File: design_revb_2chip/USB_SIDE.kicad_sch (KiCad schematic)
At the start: 53 parts, among them J1 USB_C_Receptacle, J2 Conn_01x08, U1 LAN7801-I/9JX, U2 TPS62162QDSGRQ1, U3 93C56A-I/P

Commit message: USB_Side Prelim Completion
- finished USB side with no revisions
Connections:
- net 3.3V is gone; now on net 3v3: C21.1, D2.2 (A), L2.2, R11.2, R9.2, U2.6 (VOS)
- net GPIO10: now also J2.1 (Pin_1); no longer J2.7 (Pin_7)
- net GPIO4: now also J2.7 (Pin_7); no longer J2.1 (Pin_1)
- net GPIO5: now also J2.6 (Pin_6); no longer J2.2 (Pin_2)
- net GPIO6: now also J2.5 (Pin_5); no longer J2.3 (Pin_3)
- net GPIO8: now also J2.3 (Pin_3); no longer J2.5 (Pin_5)
- net GPIO9: now also J2.2 (Pin_2); no longer J2.6 (Pin_6)
- net USB3_RXN: now reaches J1.A10 (RX2-), J1.B10 (RX1-), U1.44 (USB3_RXDM)
- net USB3_RXP: now reaches J1.A11 (RX2+), J1.B11 (RX1+), U1.43 (USB3_RXDP)
- net USB3_TXP: now reaches J1.A2 (TX1+), J1.B2 (TX2+), U1.40 (USB3_TXDP)
- net USB3_TXN: now reaches J1.A3 (TX1-), J1.B3 (TX2-), U1.41 (USB3_TXDM)
- net USB2_P: now reaches J1.A6 (D+), J1.B6 (D+), U1.38 (USB2_DP)
- net USB2_N: now reaches J1.A7 (D-), J1.B7 (D-), U1.39 (USB2_DM)
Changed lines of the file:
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@@
 	(wire
 		(pts
-			(xy 240.03 53.34) (xy 246.38 53.34)
-		)
-		(stroke
-			(width 0)
-			(type default)
-		)
-	)
-	(wire
-		(pts
 			(xy 59.69 106.68) (xy 59.69 127)
 		)
@@
 	(wire
 		(pts
-			(xy 240.03 50.8) (xy 246.38 50.8)
-		)
-		(stroke
-			(width 0)
-			(type default)
-		)
-	)
-	(wire
-		(pts
 			(xy 44.45 142.24) (xy 78.74 142.24)
 		)
@@
 	(wire
 		(pts
-			(xy 240.03 55.88) (xy 246.38 55.88)
-		)
-		(stroke
-			(width 0)
-			(type default)
-		)
-	)
-	(wire
-		(pts
 			(xy 165.1 91.44) (xy 198.12 91.44)
 		)
@@
 	(wire
 		(pts
-			(xy 240.03 45.72) (xy 246.38 45.72)
-		)
-		(stroke
-			(width 0)
-			(type default)
-		)
-	)
-	(wire
-		(pts
 			(xy 243.84 63.5) (xy 243.84 66.04)
 		)
@@
 	(wire
 		(pts
-			(xy 240.03 60.96) (xy 246.38 60.96)
-		)
-		(stroke
-			(width 0)
-			(type default)
-		)
-	)
-	(wire
-		(pts
 			(xy 39.37 243.84) (xy 52.07 243.84)
 		)
@@
 	(wire
 		(pts
-			(xy 240.03 58.42) (xy 246.38 58.42)
-		)
-		(stroke
-			(width 0)
-			(type default)
-		)
-	)
-	(wire
-		(pts
 			(xy 177.8 240.03) (xy 161.29 240.03)
 		)
@@
 	(wire
 		(pts
-			(xy 240.03 48.26) (xy 246.38 48.26)
-		)
-		(stroke
-			(width 0)
-			(type default)
-		)
-	)
-	(wire
-		(pts
 			(xy 146.05 245.11) (xy 146.05 248.92)
 		)
@@
 		)
 	)
+	(label "USB2_N"
+		(at 71.12 139.7 0)
+		(fields_autoplaced yes)
+		(effects
+			(font
+				(size 1.27 1.27)
+			)
+			(justify left bottom)
+		)
+	)
+	(label "USB3_RXP"
+		(at 57.15 129.54 0)
+		(fields_autoplaced yes)
+		(effects
+			(font
+				(size 1.27 1.27)
+			)
+			(justify left bottom)
+		)
+	)
+	(label "USB3_RXN"
+		(at 60.96 127 0)
+		(fields_autoplaced yes)
+		(effects
+			(font
+				(size 1.27 1.27)
+			)
+			(justify left bottom)
+		)
+	)
+	(label "USB3_TXP"
+		(at 53.34 137.16 0)
+		(fields_autoplaced yes)
+		(effects
+			(font
+				(size 1.27 1.27)
+			)
+			(justify left bottom)
+		)
+	)
+	(label "USB2_P"
+		(at 71.12 142.24 0)
+		(fields_autoplaced yes)
+		(effects
+			(font
+				(size 1.27 1.27)
+			)
+			(justify left bottom)
+		)
+	)
+	(label "USB3_TXN"
+		(at 57.15 134.62 0)
+		(fields_autoplaced yes)
+		(effects
+			(font
+				(size 1.27 1.27)
+			)
+			(justify left bottom)
+		)
+	)
 	(global_label "VBUS_DET"
 		(shape input)
@@
 	(global_label "GPIO5"
 		(shape input)
-		(at 240.03 48.26 180)
+		(at 246.38 58.42 180)
 		(fields_autoplaced yes)
 		(effects
@@
 		)
 		(property "Intersheetrefs" "${INTERSHEET_REFS}"
-			(at 231.36 48.26 0)
+			(at 237.71 58.42 0)
 			(effects
 				(font
@@
 	(global_label "GPIO4"
 		(shape input)
-		(at 240.03 45.72 180)
+		(at 246.38 60.96 180)
 		(fields_autoplaced yes)
 		(effects
@@
 		)
 		(property "Intersheetrefs" "${INTERSHEET_REFS}"
-			(at 231.36 45.72 0)
+			(at 237.71 60.96 0)
 			(effects
 				(font
@@
 	(global_label "GPIO10"
 		(shape input)
-		(at 240.03 60.96 180)
+		(at 246.38 45.72 180)
 		(fields_autoplaced yes)
 		(effects
@@
 		)
 		(property "Intersheetrefs" "${INTERSHEET_REFS}"
-			(at 230.1505 60.96 0)
+			(at 236.5005 45.72 0)
 			(effects
 				(font
@@
 	(global_label "GPIO6"
 		(shape input)
-		(at 240.03 50.8 180)
+		(at 246.38 55.88 180)
 		(fields_autoplaced yes)
 		(effects
@@
 		)
 		(property "Intersheetrefs" "${INTERSHEET_REFS}"
-			(at 231.36 50.8 0)
+			(at 237.71 55.88 0)
 			(effects
 				(font
@@
 	(global_label "GPIO7"
 		(shape input)
-		(at 240.03 53.34 180)
+		(at 246.38 53.34 180)
 		(fields_autoplaced yes)
 		(effects
@@
 		)
 		(property "Intersheetrefs" "${INTERSHEET_REFS}"
-			(at 231.36 53.34 0)
+			(at 237.71 53.34 0)
 			(effects
 				(font
@@
 	(global_label "GPIO8"
 		(shape input)
-		(at 240.03 55.88 180)
+		(at 246.38 50.8 180)
 		(fields_autoplaced yes)
 		(effects
@@
 		)
 		(property "Intersheetrefs" "${INTERSHEET_REFS}"
-			(at 231.36 55.88 0)
+			(at 237.71 50.8 0)
 			(effects
 				(font
@@
 	(global_label "GPIO9"
 		(shape input)
-		(at 240.03 58.42 180)
+		(at 246.38 48.26 180)
 		(fields_autoplaced yes)
 		(effects
@@
 		)
 		(property "Intersheetrefs" "${INTERSHEET_REFS}"
-			(at 231.36 58.42 0)
+			(at 237.71 48.26 0)
 			(effects
 				(font
@@
 		(shape input)
 		(at 198.12 93.98 0)
+		(fields_autoplaced yes)
 		(effects
 			(font
@@
 		(shape input)
 		(at 198.12 109.22 0)
+		(fields_autoplaced yes)
 		(effects
 			(font
@@
 		(shape input)
 		(at 78.74 96.52 180)
+		(fields_autoplaced yes)
 		(effects
 			(font
@@
 		(shape input)
 		(at 198.12 81.28 0)
+		(fields_autoplaced yes)
 		(effects
 			(font
@@
 		(shape input)
 		(at 198.12 86.36 0)
+		(fields_autoplaced yes)
 		(effects
 			(font
@@
 		(shape input)
 		(at 198.12 91.44 0)
+		(fields_autoplaced yes)
 		(effects
 			(font
@@
 		(shape input)
 		(at 198.12 96.52 0)
+		(fields_autoplaced yes)
 		(effects
 			(font
@@
 		(shape input)
 		(at 165.1 149.86 0)
+		(fields_autoplaced yes)
 		(effects
 			(font
@@
 		(shape input)
 		(at 198.12 106.68 0)
+		(fields_autoplaced yes)
 		(effects
 			(font
@@
 		(shape input)
 		(at 198.12 114.3 0)
+		(fields_autoplaced yes)
 		(effects
 			(font
@@
 		(shape input)
 		(at 165.1 152.4 0)
+		(fields_autoplaced yes)
 		(effects
 			(font
@@
 		(shape input)
 		(at 198.12 111.76 0)
+		(fields_autoplaced yes)
 		(effects
 			(font
@@
 		(shape input)
 		(at 66.04 100.33 270)
+		(fields_autoplaced yes)
 		(effects
 			(font
@@
 		(shape input)
 		(at 78.74 83.82 180)
+		(fields_autoplaced yes)
 		(effects
 			(font
@@
 		(shape input)
 		(at 198.12 104.14 0)
+		(fields_autoplaced yes)
 		(effects
 			(font
@@
 		(shape input)
 		(at 198.12 83.82 0)
+		(fields_autoplaced yes)
 		(effects
 			(font
@@
 		(shape input)
 		(at 198.12 101.6 0)
+		(fields_autoplaced yes)
 		(effects
 			(font
@@
 			)
 		)
-		(property "Value" "3.3V"
+		(property "Value" "3v3"
 			(at 266.7 227.33 0)
 			(effects

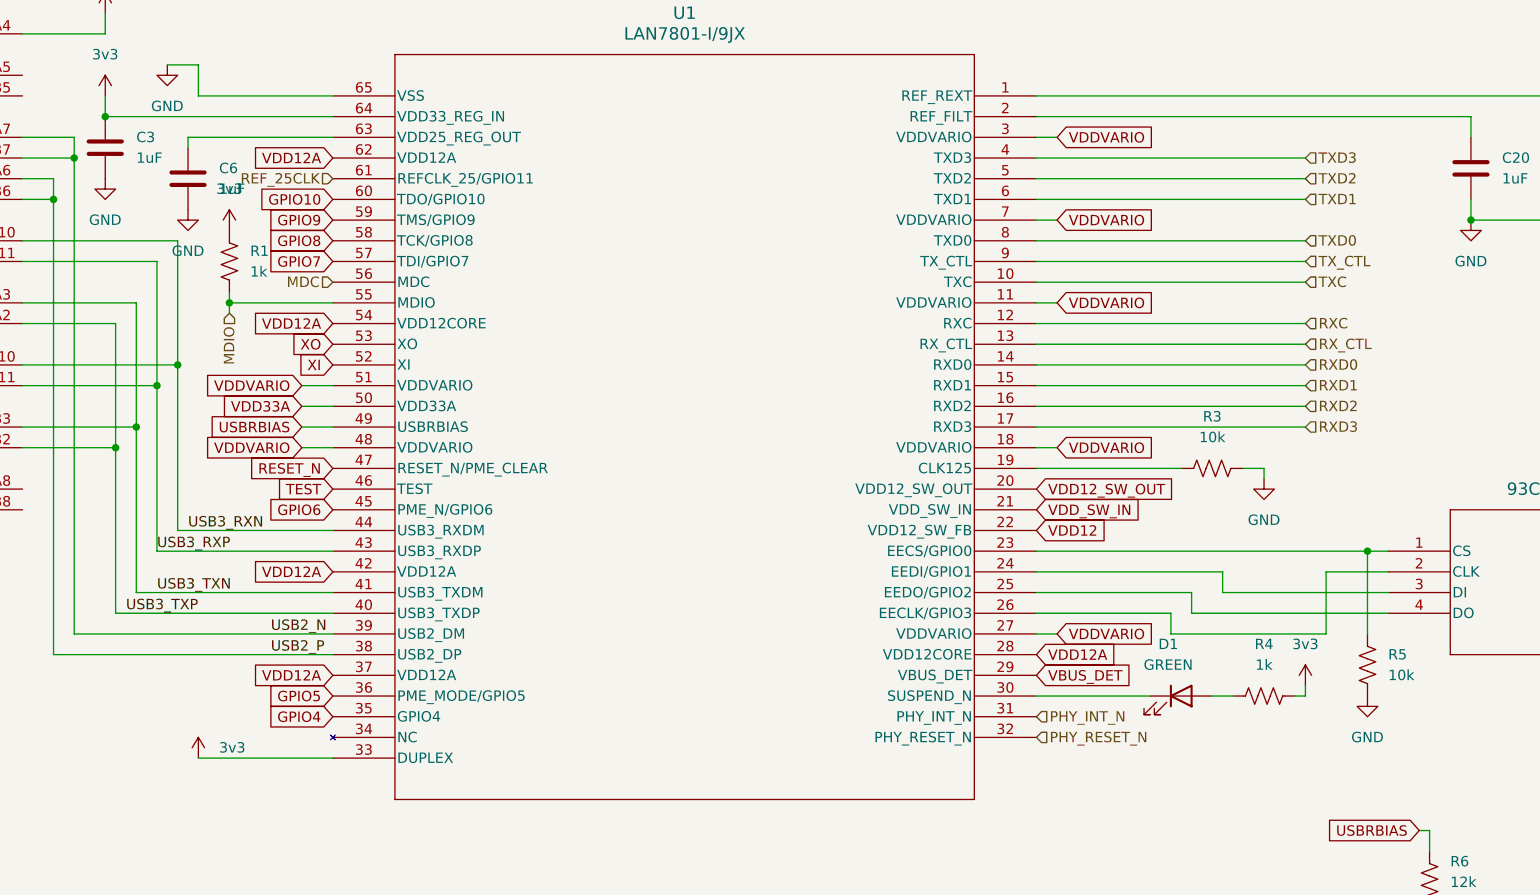
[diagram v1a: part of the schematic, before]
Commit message: routing eth side
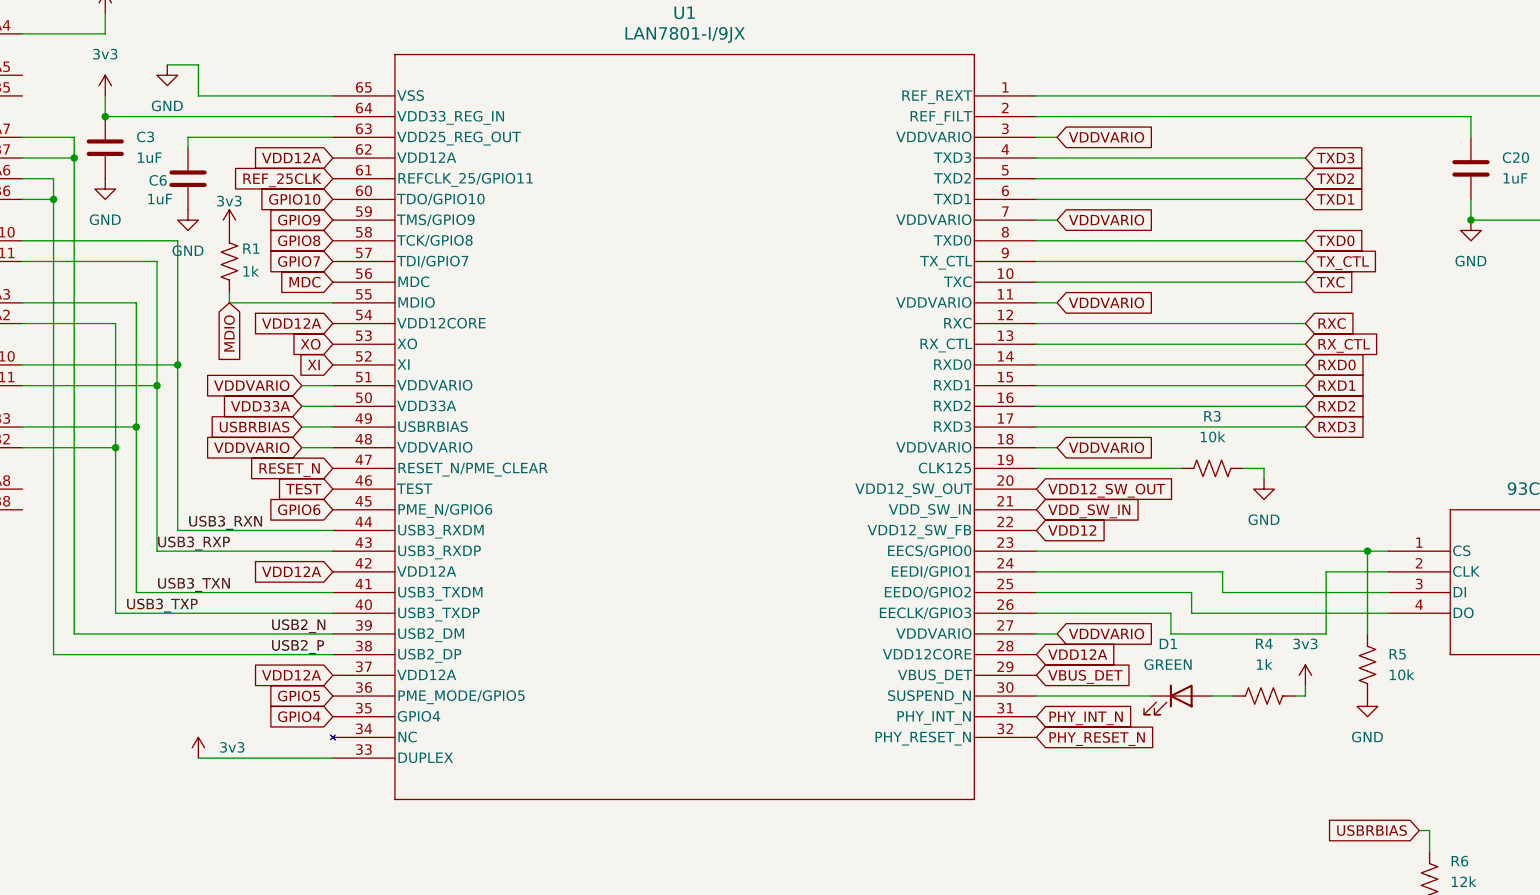
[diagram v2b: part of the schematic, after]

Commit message: Final PCB Fixes
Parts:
- removed J1: USB_C_Receptacle, Connector_USB:USB_C_Receptacle_Molex_105450-0101, symbol Connector:USB_C_Receptacle
- added J4: UJ31-CH-3-SMT-TR, Capstone_Footprints:CUI_UJ31-CH-3-SMT-TR, symbol Capstone_Synbols:UJ31-CH-3-SMT-TR
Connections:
- net GND: now also J4.A1 (GND), J4.A12 (GND__1), J4.B1 (GND__2), J4.B12 (GND__3)
- net USB2_N: now also J4.A7 (DN1), J4.B7 (DN2)
- net USB2_P: now also J4.A6 (DP1), J4.B6 (DP2)
- net USB3_RXN: now also J4.A10 (SSRXN2), J4.B10 (SSRXN1)
- net USB3_RXP: now also J4.A11 (SSRXP2), J4.B11 (SSRXP1)
- net USB3_TXN: now also J4.A3 (SSTXN1), J4.B3 (SSTXN2)
- net USB3_TXP: now also J4.A2 (SSTXP1), J4.B2 (SSTXP2)
- net USB_SHIELD: now also J4.SH1 (SHIELD), J4.SH2 (SHIELD__1), J4.SH3 (SHIELD__2), J4.SH4 (SHIELD__3)
- net VBUS: now also J4.A4 (VBUS), J4.A9 (VBUS__1), J4.B4 (VBUS__2), J4.B9 (VBUS__3)

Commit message: footprint resizing
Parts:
- C1, C10, C11, C12, C14, C15, C17, C19, C2, C20, C22, C23, C24, C25, C26, C4, C5, C6, C7, C8, C9: footprint Capacitor_SMD:C_0201_0603Metric -> Capacitor_SMD:C_0402_1005Metric
- C13, C16, C18, C21, C3: footprint Capacitor_SMD:C_0201_0603Metric -> Capacitor_SMD:C_0603_1608Metric
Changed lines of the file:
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@@
 			)
 		)
-		(property "Footprint" "Capacitor_SMD:C_0201_0603Metric"
+		(property "Footprint" "Capacitor_SMD:C_0402_1005Metric"
 			(at 53.0352 243.84 0)
 			(effects
@@
 			)
 		)
-		(property "Footprint" "Capacitor_SMD:C_0201_0603Metric"
+		(property "Footprint" "Capacitor_SMD:C_0402_1005Metric"
 			(at 61.9252 87.63 0)
 			(effects
@@
 			)
 		)
-		(property "Footprint" "Capacitor_SMD:C_0201_0603Metric"
+		(property "Footprint" "Capacitor_SMD:C_0402_1005Metric"
 			(at 65.7352 243.84 0)
 			(effects
@@
 			)
 		)
-		(property "Footprint" "Capacitor_SMD:C_0201_0603Metric"
+		(property "Footprint" "Capacitor_SMD:C_0402_1005Metric"
 			(at 55.5752 195.58 0)
 			(effects
@@
 			)
 		)
-		(property "Footprint" "Capacitor_SMD:C_0201_0603Metric"
+		(property "Footprint" "Capacitor_SMD:C_0603_1608Metric"
 			(at 105.1052 203.2 0)
 			(effects
@@
 			)
 		)
-		(property "Footprint" "Capacitor_SMD:C_0201_0603Metric"
+		(property "Footprint" "Capacitor_SMD:C_0402_1005Metric"
 			(at 89.8652 195.58 0)
 			(effects
@@
 			)
 		)
-		(property "Footprint" "Capacitor_SMD:C_0201_0603Metric"
+		(property "Footprint" "Capacitor_SMD:C_0603_1608Metric"
 			(at 256.2352 248.92 0)
 			(effects
@@
 			)
 		)
-		(property "Footprint" "Capacitor_SMD:C_0201_0603Metric"
+		(property "Footprint" "Capacitor_SMD:C_0402_1005Metric"
 			(at 106.3752 243.84 0)
 			(effects
@@
 			)
 		)
-		(property "Footprint" "Capacitor_SMD:C_0201_0603Metric"
+		(property "Footprint" "Capacitor_SMD:C_0402_1005Metric"
 			(at 78.4352 243.84 0)
 			(effects
@@
 			)
 		)
-		(property "Footprint" "Capacitor_SMD:C_0201_0603Metric"
+		(property "Footprint" "Capacitor_SMD:C_0402_1005Metric"
 			(at 268.9352 140.97 0)
 			(effects
@@
 			)
 		)
-		(property "Footprint" "Capacitor_SMD:C_0201_0603Metric"
+		(property "Footprint" "Capacitor_SMD:C_0402_1005Metric"
 			(at 219.4052 86.36 0)
 			(effects
@@
 			)
 		)
-		(property "Footprint" "Capacitor_SMD:C_0201_0603Metric"
+		(property "Footprint" "Capacitor_SMD:C_0402_1005Metric"
 			(at 318.4652 143.51 0)
 			(effects
@@
 			)
 		)
-		(property "Footprint" "Capacitor_SMD:C_0201_0603Metric"
+		(property "Footprint" "Capacitor_SMD:C_0402_1005Metric"
 			(at 187.6552 191.77 0)
 			(effects
@@
 			)
 		)
-		(property "Footprint" "Capacitor_SMD:C_0201_0603Metric"
+		(property "Footprint" "Capacitor_SMD:C_0402_1005Metric"
 			(at 318.4652 194.31 0)
 			(effects
@@
 			)
 		)
-		(property "Footprint" "Capacitor_SMD:C_0201_0603Metric"
+		(property "Footprint" "Capacitor_SMD:C_0402_1005Metric"
 			(at 120.3452 243.84 0)
 			(effects
@@
 			)
 		)
-		(property "Footprint" "Capacitor_SMD:C_0201_0603Metric"
+		(property "Footprint" "Capacitor_SMD:C_0402_1005Metric"
 			(at 44.1452 195.58 0)
 			(effects
@@
 			)
 		)
-		(property "Footprint" "Capacitor_SMD:C_0201_0603Metric"
+		(property "Footprint" "Capacitor_SMD:C_0402_1005Metric"
 			(at 40.3352 243.84 0)
 			(effects
@@
 			)
 		)
-		(property "Footprint" "Capacitor_SMD:C_0201_0603Metric"
+		(property "Footprint" "Capacitor_SMD:C_0402_1005Metric"
 			(at 162.2552 248.92 0)
 			(effects
@@
 			)
 		)
-		(property "Footprint" "Capacitor_SMD:C_0201_0603Metric"
+		(property "Footprint" "Capacitor_SMD:C_0402_1005Metric"
 			(at 67.0052 195.58 0)
 			(effects
@@
 			)
 		)
-		(property "Footprint" "Capacitor_SMD:C_0201_0603Metric"
+		(property "Footprint" "Capacitor_SMD:C_0402_1005Metric"
 			(at 354.0252 148.59 0)
 			(effects
@@
 			)
 		)
-		(property "Footprint" "Capacitor_SMD:C_0201_0603Metric"
+		(property "Footprint" "Capacitor_SMD:C_0603_1608Metric"
 			(at 51.7652 83.82 0)
 			(effects
@@
 			)
 		)
-		(property "Footprint" "Capacitor_SMD:C_0201_0603Metric"
+		(property "Footprint" "Capacitor_SMD:C_0402_1005Metric"
 			(at 78.4352 195.58 0)
 			(effects
@@
 			)
 		)
-		(property "Footprint" "Capacitor_SMD:C_0201_0603Metric"
+		(property "Footprint" "Capacitor_SMD:C_0402_1005Metric"
 			(at 265.1252 180.34 0)
 			(effects
@@
 			)
 		)
-		(property "Footprint" "Capacitor_SMD:C_0201_0603Metric"
+		(property "Footprint" "Capacitor_SMD:C_0603_1608Metric"
 			(at 174.9552 191.77 0)
 			(effects
@@
 			)
 		)
-		(property "Footprint" "Capacitor_SMD:C_0201_0603Metric"
+		(property "Footprint" "Capacitor_SMD:C_0402_1005Metric"
 			(at 92.4052 243.84 0)
 			(effects
@@
 			)
 		)
-		(property "Footprint" "Capacitor_SMD:C_0201_0603Metric"
+		(property "Footprint" "Capacitor_SMD:C_0603_1608Metric"
 			(at 147.0152 245.11 0)
 			(effects

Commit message: Final Push for Rev A 1.0
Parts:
- C13, C16, C21: footprint Capacitor_SMD:C_0603_1608Metric -> Capacitor_SMD:C_0805_2012Metric
- C3: footprint Capacitor_SMD:C_0603_1608Metric -> Capacitor_SMD:C_0402_1005Metric
- L1: footprint Inductor_SMD_Wurth:L_Wurth_WE-LQSH-3012 -> Inductor_SMD:L_0603_1608Metric
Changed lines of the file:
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@@
 	(label "USB2_N"
 		(at 71.12 139.7 0)
+		(fields_autoplaced yes)
 		(effects
 			(font
@@
 	(label "USB3_RXP"
 		(at 57.15 129.54 0)
+		(fields_autoplaced yes)
 		(effects
 			(font
@@
 	(label "USB3_RXN"
 		(at 60.96 127 0)
+		(fields_autoplaced yes)
 		(effects
 			(font
@@
 	(label "USB3_TXP"
 		(at 53.34 137.16 0)
+		(fields_autoplaced yes)
 		(effects
 			(font
@@
 	(label "USB2_P"
 		(at 71.12 142.24 0)
+		(fields_autoplaced yes)
 		(effects
 			(font
@@
 	(label "USB3_TXN"
 		(at 57.15 134.62 0)
+		(fields_autoplaced yes)
 		(effects
 			(font
@@
 			)
 		)
-		(property "Footprint" "Inductor_SMD_Wurth:L_Wurth_WE-LQSH-3012"
+		(property "Footprint" "Inductor_SMD:L_0603_1608Metric"
 			(at 111.76 194.31 0)
 			(effects
@@
 			)
 		)
-		(property "Footprint" "Capacitor_SMD:C_0603_1608Metric"
+		(property "Footprint" "Capacitor_SMD:C_0805_2012Metric"
 			(at 105.1052 203.2 0)
 			(effects
@@
 			)
 		)
-		(property "Footprint" "Capacitor_SMD:C_0603_1608Metric"
+		(property "Footprint" "Capacitor_SMD:C_0805_2012Metric"
 			(at 256.2352 248.92 0)
 			(effects
@@
 			)
 		)
-		(property "Footprint" "Capacitor_SMD:C_0603_1608Metric"
+		(property "Footprint" "Capacitor_SMD:C_0402_1005Metric"
 			(at 51.7652 83.82 0)
 			(effects
@@
 			)
 		)
-		(property "Footprint" "Capacitor_SMD:C_0603_1608Metric"
+		(property "Footprint" "Capacitor_SMD:C_0805_2012Metric"
 			(at 147.0152 245.11 0)
 			(effects
